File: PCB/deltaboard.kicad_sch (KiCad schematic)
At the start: 310 parts, among them J1 USB_C_Receptacle, J2 Conn_01x04, K1 Esc, K10 F9, K11 F10, K12 F11, K13 F12, K14 Blank, K15 Blank, K16 ~~,`, K17 !,1, K18 @,2, K19 #,3, K2 F1, K20 $,4, K21 %,5, K22 ^,6, K23 &,7, K24 *,8, K25 (,9, K26 ),0, K27 _,-, K28 +,=, K29 Backspace, K3 F2, K30 Insert, K31 Home, K33 Tab, K34 Q, K35 W, K36 E, K37 R, K38 T, K39 Y, K4 F3, K40 U, K41 I, K42 O, K43 P, K44 {,[, K45 },], K46 |,\, K47 Delete, K48 End, K49 PgUp, K5 F4, K50 Caps Lock, K51 A, K52 S, K53 D, K54 F, K55 G, K56 H, K57 J, K58 K, K59 L, K6 F5, K60 :,;, K61 ",', K62 Enter, K63 Shift, K64 Z, K65 X, K66 C, K67 V, K68 B, K69 N, K7 F6, K70 M, K71 <,,, K72 >,., K73 ?,/, K74 Shift, K75 ↑, K76 Ctrl, K77 Win, K78 Alt, K79 Blank, K8 F7, K80 Alt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

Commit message: finalize pcb design
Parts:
- added H10, H11, H9: MountingHole, MountingHole:MountingHole_2.7mm_M2.5, symbol Mechanical:MountingHole
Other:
- moved on the sheet: H1, H2, H3, H4, H5, H6, H7, H8

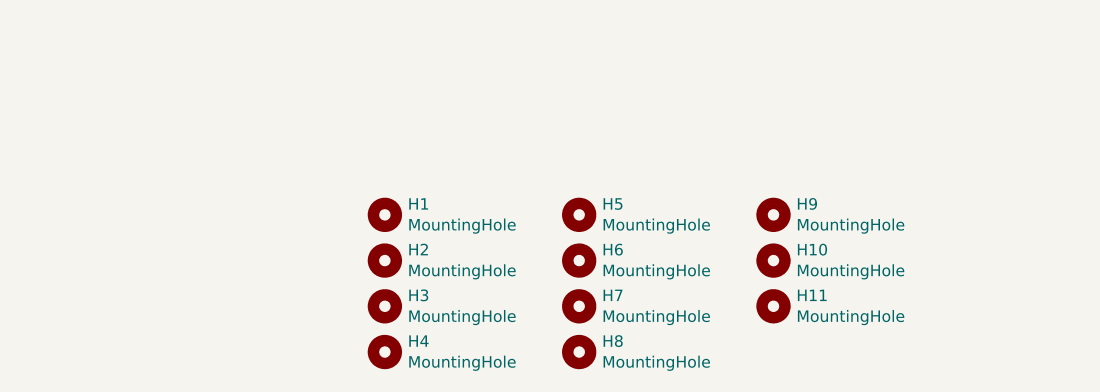
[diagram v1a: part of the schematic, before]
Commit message: feat: add more mounting holes
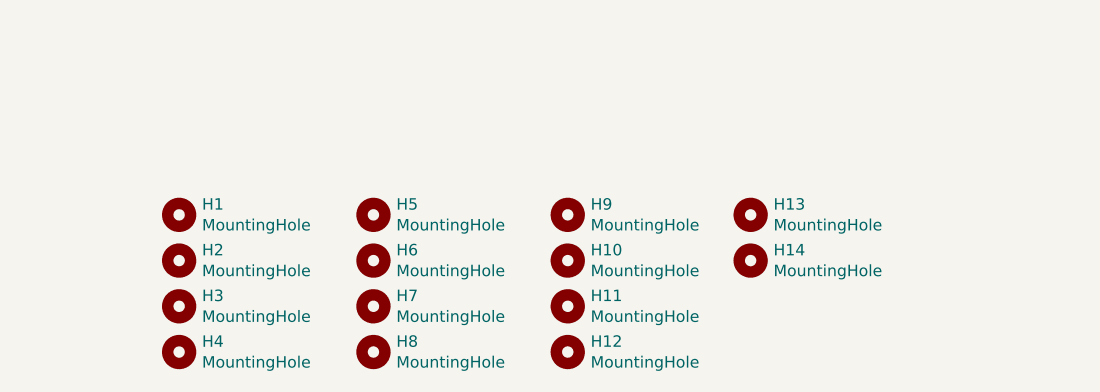
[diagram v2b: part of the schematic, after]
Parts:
- added H12, H13, H14: MountingHole, MountingHole:MountingHole_2.7mm_M2.5, symbol Mechanical:MountingHole
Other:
- moved on the sheet: H1, H10, H11, H2, H3, H4, H5, H6, H7, H8, H9

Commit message: generate initial production files
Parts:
- H1, H10, H11, H12, H13, H14, H2, H3, H4, H5, H6, H7, H8, H9: footprint MountingHole:MountingHole_2.7mm_M2.5 -> MountingHole:MountingHole_3.2mm_M3
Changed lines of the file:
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@@
 			)
 		)
-		(property "Footprint" "MountingHole:MountingHole_2.7mm_M2.5"
+		(property "Footprint" "MountingHole:MountingHole_3.2mm_M3"
 			(at 389.89 386.08 0)
 			(effects
@@
 			)
 		)
-		(property "Footprint" "MountingHole:MountingHole_2.7mm_M2.5"
+		(property "Footprint" "MountingHole:MountingHole_3.2mm_M3"
 			(at 389.89 391.16 0)
 			(effects
@@
 			)
 		)
-		(property "Footprint" "MountingHole:MountingHole_2.7mm_M2.5"
+		(property "Footprint" "MountingHole:MountingHole_3.2mm_M3"
 			(at 389.89 396.24 0)
 			(effects
@@
 			)
 		)
-		(property "Footprint" "MountingHole:MountingHole_2.7mm_M2.5"
+		(property "Footprint" "MountingHole:MountingHole_3.2mm_M3"
 			(at 389.89 401.32 0)
 			(effects
@@
 			)
 		)
-		(property "Footprint" "MountingHole:MountingHole_2.7mm_M2.5"
+		(property "Footprint" "MountingHole:MountingHole_3.2mm_M3"
 			(at 433.07 396.24 0)
 			(effects
@@
 			)
 		)
-		(property "Footprint" "MountingHole:MountingHole_2.7mm_M2.5"
+		(property "Footprint" "MountingHole:MountingHole_3.2mm_M3"
 			(at 411.48 391.16 0)
 			(effects
@@
 			)
 		)
-		(property "Footprint" "MountingHole:MountingHole_2.7mm_M2.5"
+		(property "Footprint" "MountingHole:MountingHole_3.2mm_M3"
 			(at 411.48 386.08 0)
 			(effects
@@
 			)
 		)
-		(property "Footprint" "MountingHole:MountingHole_2.7mm_M2.5"
+		(property "Footprint" "MountingHole:MountingHole_3.2mm_M3"
 			(at 433.07 401.32 0)
 			(effects
@@
 			)
 		)
-		(property "Footprint" "MountingHole:MountingHole_2.7mm_M2.5"
+		(property "Footprint" "MountingHole:MountingHole_3.2mm_M3"
 			(at 453.39 386.08 0)
 			(effects
@@
 			)
 		)
-		(property "Footprint" "MountingHole:MountingHole_2.7mm_M2.5"
+		(property "Footprint" "MountingHole:MountingHole_3.2mm_M3"
 			(at 411.48 396.24 0)
 			(effects
@@
 			)
 		)
-		(property "Footprint" "MountingHole:MountingHole_2.7mm_M2.5"
+		(property "Footprint" "MountingHole:MountingHole_3.2mm_M3"
 			(at 433.07 386.08 0)
 			(effects
@@
 			)
 		)
-		(property "Footprint" "MountingHole:MountingHole_2.7mm_M2.5"
+		(property "Footprint" "MountingHole:MountingHole_3.2mm_M3"
 			(at 433.07 391.16 0)
 			(effects
@@
 			)
 		)
-		(property "Footprint" "MountingHole:MountingHole_2.7mm_M2.5"
+		(property "Footprint" "MountingHole:MountingHole_3.2mm_M3"
 			(at 453.39 391.16 0)
 			(effects
@@
 			)
 		)
-		(property "Footprint" "MountingHole:MountingHole_2.7mm_M2.5"
+		(property "Footprint" "MountingHole:MountingHole_3.2mm_M3"
 			(at 411.48 401.32 0)
 			(effects
